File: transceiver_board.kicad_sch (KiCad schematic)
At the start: 0 parts

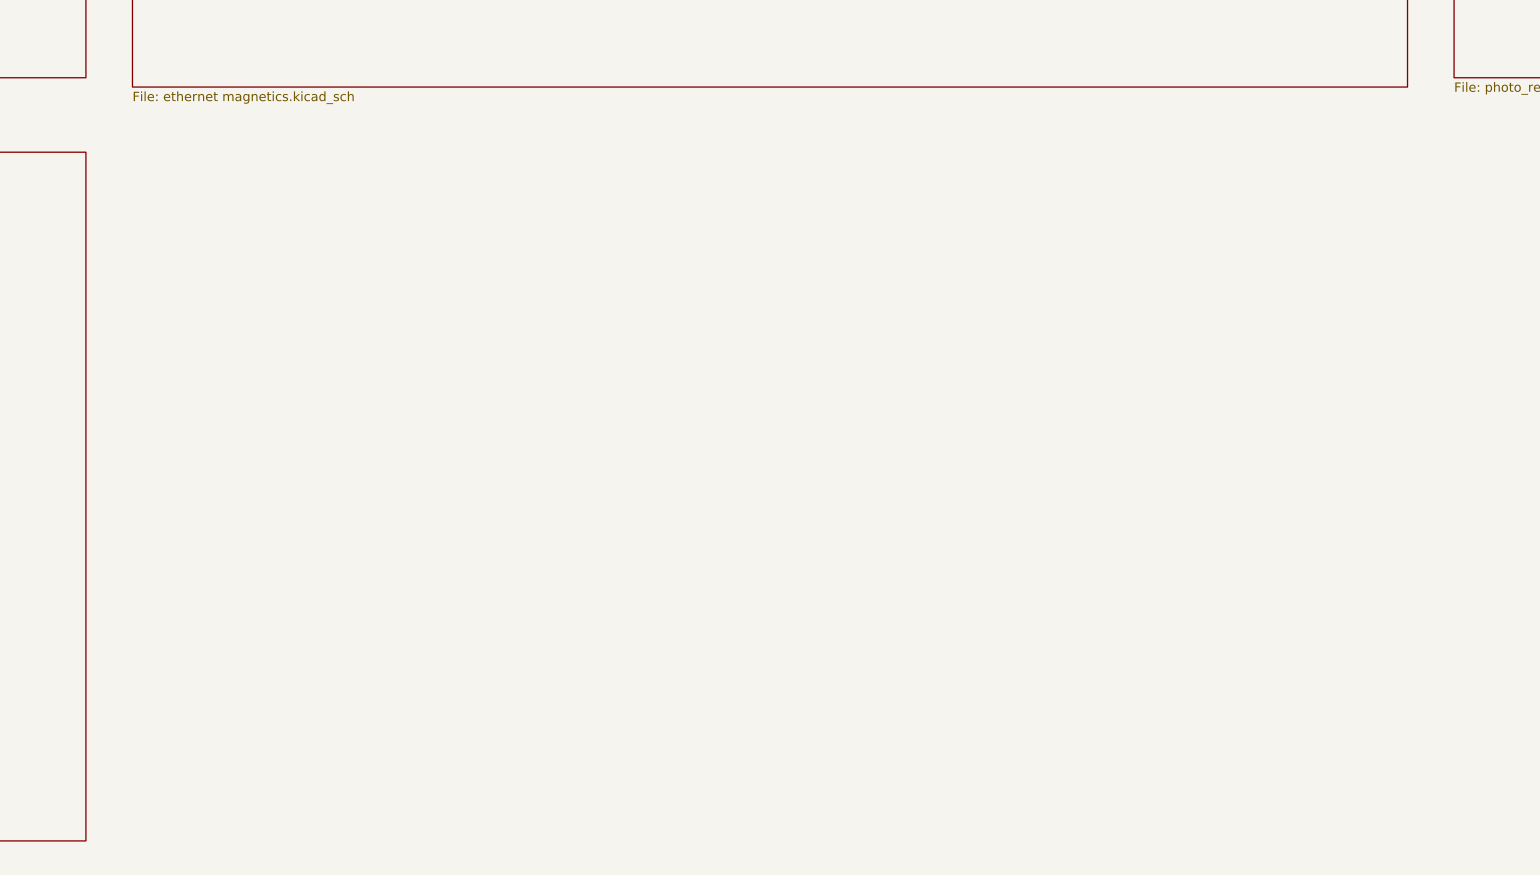
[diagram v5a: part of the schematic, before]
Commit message: add laser transmitter circuitry
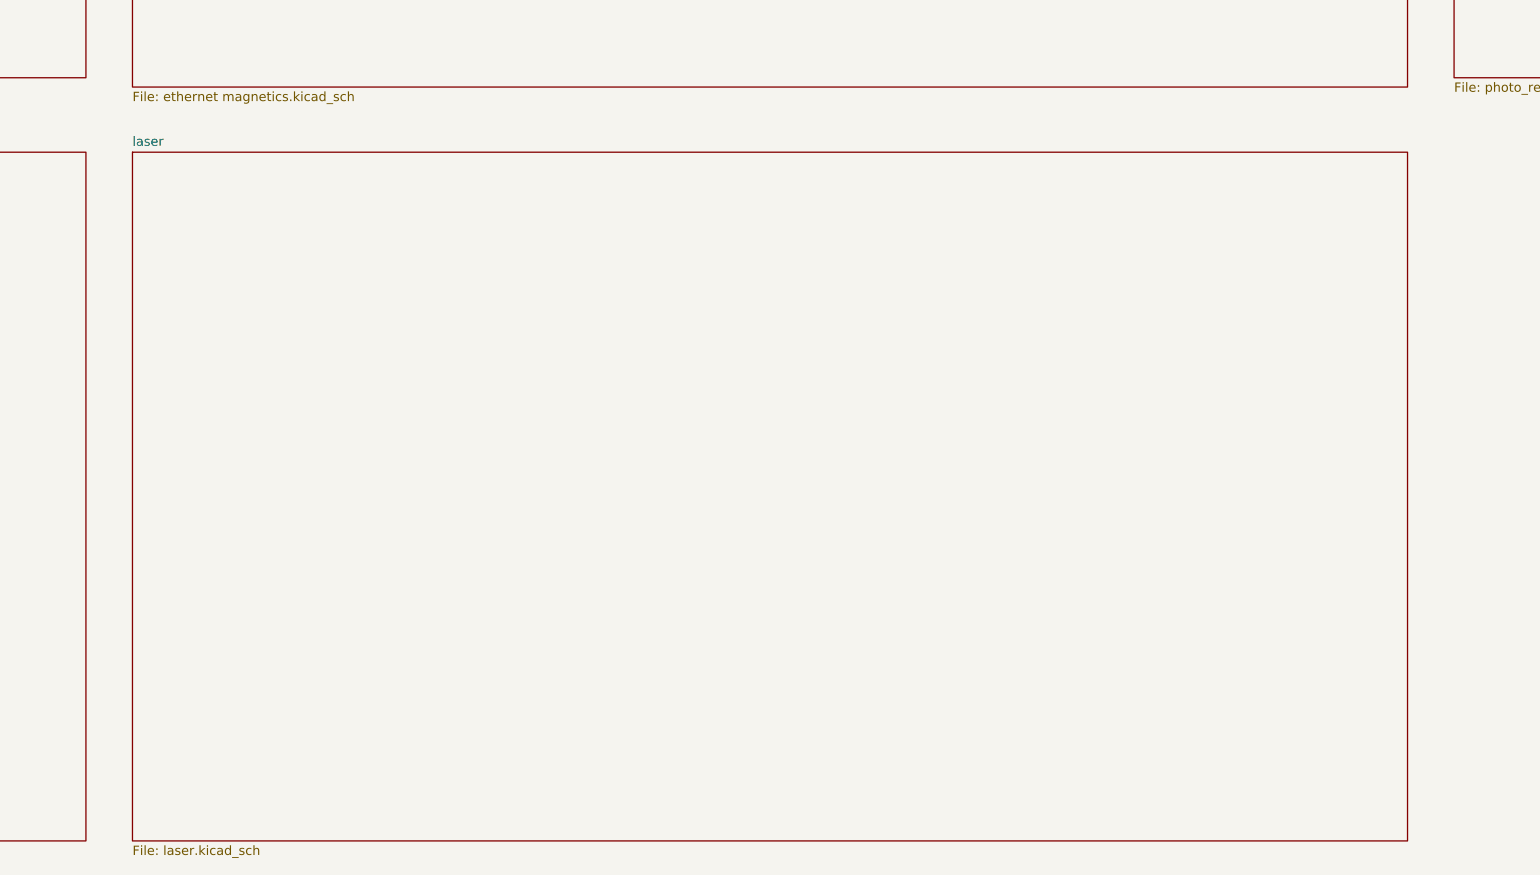
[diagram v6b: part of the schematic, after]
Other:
- added sheet laser (laser.kicad_sch)
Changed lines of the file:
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@@
+    )
+  )
+  (sheet (at 208.28 254) (size 173.99 93.98) (fields_autoplaced)
+    (stroke (width 0.1524) (type solid) (color 0 0 0 0))
+    (fill (color 0 0 0 0.0000))
+    (property "Sheet name" "laser" (id 0) (at 208.28 253.2884 0)
+      (effects (font (size 1.27 1.27)) (justify left bottom))
+    )
+    (property "Sheet file" "laser.kicad_sch" (id 1) (at 208.28 348.5646 0)
+      (effects (font (size 1.27 1.27)) (justify left top))
     )
   )
@@
     (path "/9c91d18d-68d4-4932-8503-e5dad9f3ecb3" (page "7"))
     (path "/099fbc0b-58f5-4ea0-91be-48e4a94d6545" (page "8"))
+    (path "/1de94cad-76c0-4a30-84fe-02d514b058e5" (page "9"))
   )
   (symbol_instances
@@
       (reference "#PWR0101") (unit 1) (value "GND") (footprint "")
     )
+    (path "/1de94cad-76c0-4a30-84fe-02d514b058e5/f9afb48e-fa33-48d5-9928-f6054fb650bc"
+      (reference "#PWR?") (unit 1) (value "GND") (footprint "")
+    )
     (path "/ba74941e-d0cd-46a4-ade7-f1aec57ffafc/37390626-ae04-4360-9ff8-4cc9e030e613"
       (reference "C1") (unit 1) (value "0.1u") (footprint "")
@@
       (reference "J2") (unit 1) (value "Conn_01x02_Male") (footprint "")
     )
+    (path "/1de94cad-76c0-4a30-84fe-02d514b058e5/4725cdc7-9cc0-4c76-8edc-0dc2cb0031f3"
+      (reference "J?") (unit 1) (value "Conn_Coaxial") (footprint "")
+    )
     (path "/8e682951-d8d0-4614-a72d-99ac2c01b394/dd09f115-e700-459a-8325-2ba379bc053e"
       (reference "JP1") (unit 1) (value "SolderJumper_2_Open") (footprint "")
@@
       (reference "PhotoReceiver1") (unit 1) (value "FDS010") (footprint "")
     )
+    (path "/1de94cad-76c0-4a30-84fe-02d514b058e5/828d5737-58d6-402a-8f28-c69582938413"
+      (reference "Q?") (unit 1) (value "BC547") (footprint "Package_TO_SOT_THT:TO-92_Inline")
+    )
+    (path "/1de94cad-76c0-4a30-84fe-02d514b058e5/92d08138-ad32-438e-a266-e2fff0798662"
+      (reference "Q?") (unit 1) (value "BC547") (footprint "Package_TO_SOT_THT:TO-92_Inline")
+    )
     (path "/ba74941e-d0cd-46a4-ade7-f1aec57ffafc/1996c559-3c89-4ba6-bd00-1cb04a42d3ce"
